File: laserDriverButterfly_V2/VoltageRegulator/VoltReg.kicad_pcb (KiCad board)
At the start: 2 copper layers, 50 x 32 mm, 22 parts, among them U1 LM317_3PinPackage, U2 IRF5852PbF, U3 LP3878MR-ADJ_NOPB

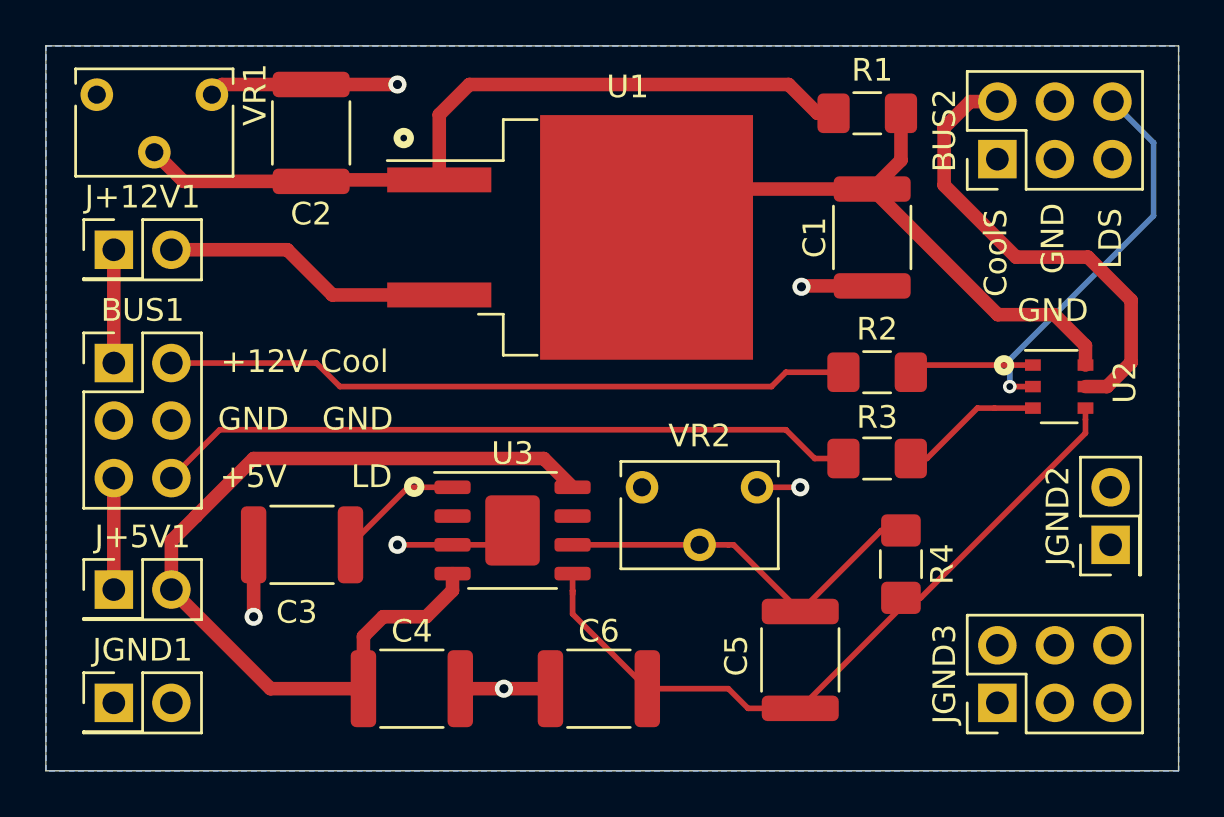
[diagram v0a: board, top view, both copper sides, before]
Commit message: update voltreg and motherboard
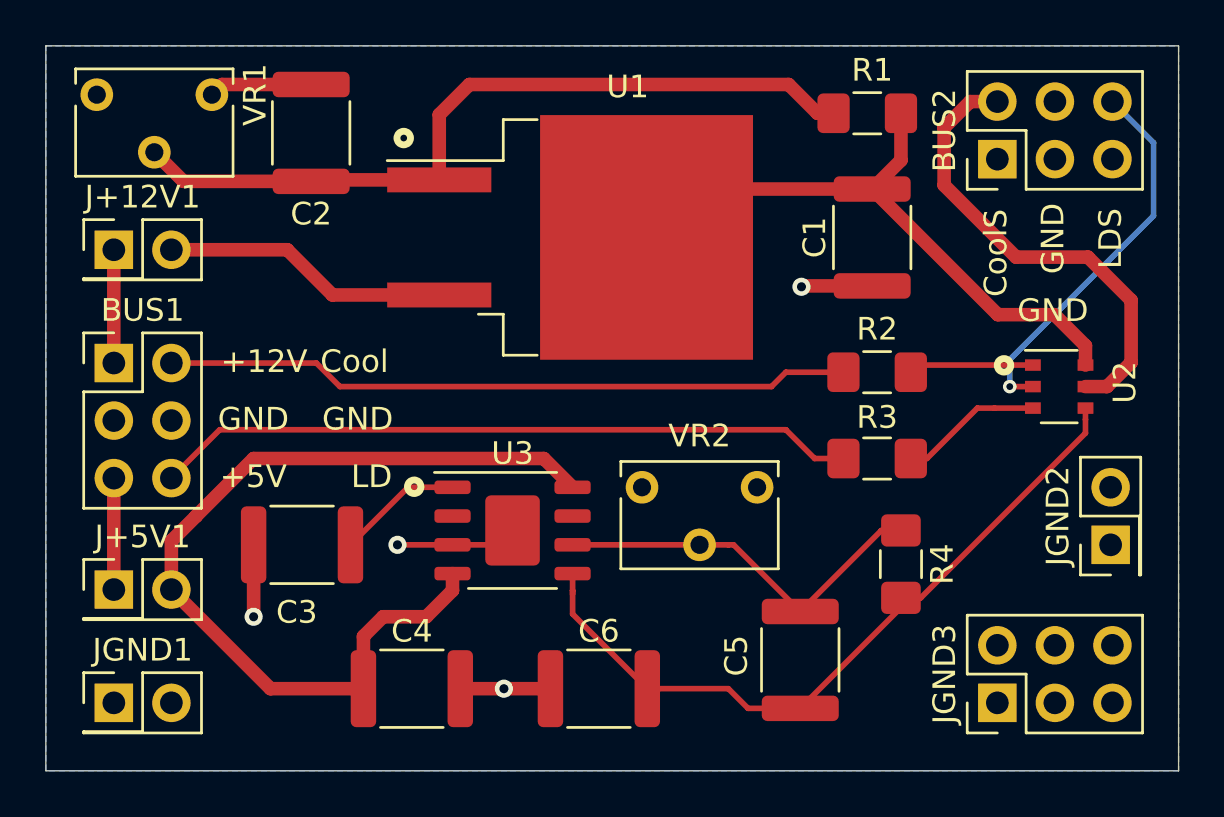
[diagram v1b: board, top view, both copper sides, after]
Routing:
- net GND: track 26.0 -> 20.3 mm, vias 6 -> 4
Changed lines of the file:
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@@
     (thickness 1.6)
     (drawings 17)
-    (tracks 106)
+    (tracks 102)
     (zones 0)
     (modules 22)
@@
     (pcbplotparams
       (layerselection 0x010fc_ffffffff)
-      (usegerberextensions false)
+      (usegerberextensions true)
       (usegerberattributes false)
       (usegerberadvancedattributes false)
@@
       (outputformat 1)
       (mirror false)
-      (drillshape 1)
+      (drillshape 0)
       (scaleselection 1)
-      (outputdirectory ""))
+      (outputdirectory "AAB_NTK4_VoltReg_Gerbers/"))
   )
   (net 0 "")
@@
   (gr_line (start 81 51) (end 81 83) (layer Edge.Cuts) (width 0.05))
   (gr_line (start 131 83) (end 131 51) (layer Edge.Cuts) (width 0.05))
-  (via (at 114.353 61.6345) (size 0.8) (drill 0.4) (layers F.Cu B.Cu) (net 3))
-  (via (at 114.3 70.485) (size 0.8) (drill 0.4) (layers F.Cu B.Cu) (net 3))
-  (via (at 96.52 52.705) (size 0.8) (drill 0.4) (layers F.Cu B.Cu) (net 3))
-  (via (at 96.52 73.025) (size 0.8) (drill 0.4) (layers F.Cu B.Cu) (net 3))
-  (via (at 90.17 76.2) (size 0.8) (drill 0.4) (layers F.Cu B.Cu) (net 3))
   (segment (start 84 70.08) (end 84 75) (width 0.6) (layer F.Cu) (net 1))
   (segment (start 114.935 69.215) (end 116.205 69.215) (width 0.25) (layer F.Cu) (net 2))
@@
   (segment (start 88.675 67.945) (end 113.665 67.945) (width 0.25) (layer F.Cu) (net 2))
   (segment (start 86.54 70.08) (end 88.675 67.945) (width 0.25) (layer F.Cu) (net 2))
+  (via (at 114.353 61.6345) (size 0.8) (drill 0.4) (layers F.Cu B.Cu) (net 3))
+  (via (at 96.52 73.025) (size 0.8) (drill 0.4) (layers F.Cu B.Cu) (net 3))
+  (via (at 90.17 76.2) (size 0.8) (drill 0.4) (layers F.Cu B.Cu) (net 3))
   (segment (start 90.17 76.2) (end 90.17 73.025) (width 0.6) (layer F.Cu) (net 3))
-  (segment (start 92.71 52.705) (end 96.52 52.705) (width 0.6) (layer F.Cu) (net 3))
   (segment (start 128.08 73.105) (end 128 73.025) (width 0.25) (layer F.Cu) (net 3))
   (segment (start 114.3925 61.595) (end 114.353 61.6345) (width 0.6) (layer F.Cu) (net 3))
@@
   (segment (start 88.778 52.705) (end 88.328 53.155) (width 0.6) (layer F.Cu) (net 3))
   (segment (start 92.71 52.705) (end 88.778 52.705) (width 0.6) (layer F.Cu) (net 3))
-  (segment (start 112.395 70.485) (end 114.3 70.485) (width 0.25) (layer F.Cu) (net 3))
   (segment (start 84 65) (end 84 60) (width 0.6) (layer F.Cu) (net 4))
   (segment (start 92.94 65) (end 86.54 65) (width 0.25) (layer F.Cu) (net 5))
@@
     (fill yes (arc_segments 32) (thermal_gap 0.508) (thermal_bridge_width 0.508))
     (polygon
-      (pts
-        (xy 131 83) (xy 81 83) (xy 81 51) (xy 131 51)
-      )
-    )
-  )
-  (zone (net 3) (net_name GND) (layer B.Cu) (hatch edge 0.508)
-    (connect_pads (clearance 0.508))
-    (min_thickness 0.127)
-    (fill yes (arc_segments 32) (thermal_gap 0.508) (thermal_bridge_width 0.508))
-    (polygon
